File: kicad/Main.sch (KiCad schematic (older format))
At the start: 0 parts

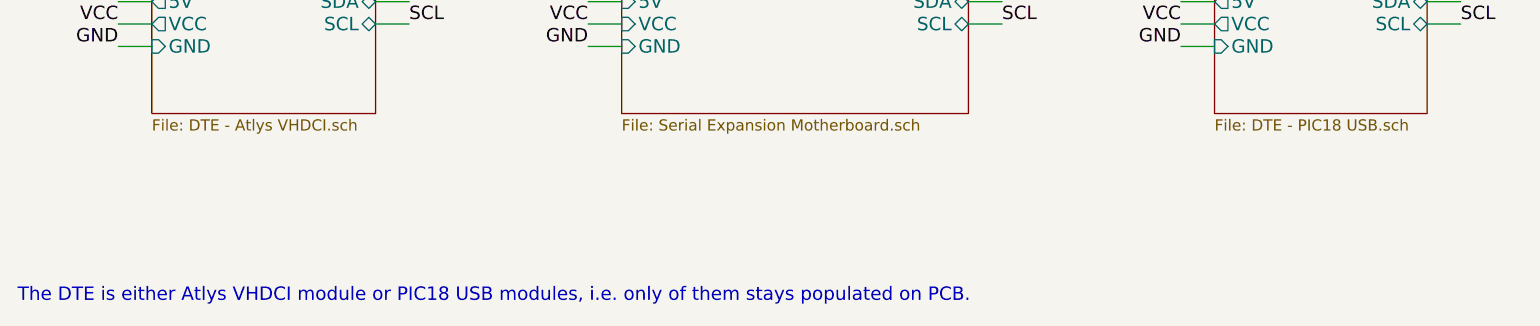
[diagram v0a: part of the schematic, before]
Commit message: ID controller complete, bypass caps added in data isolation
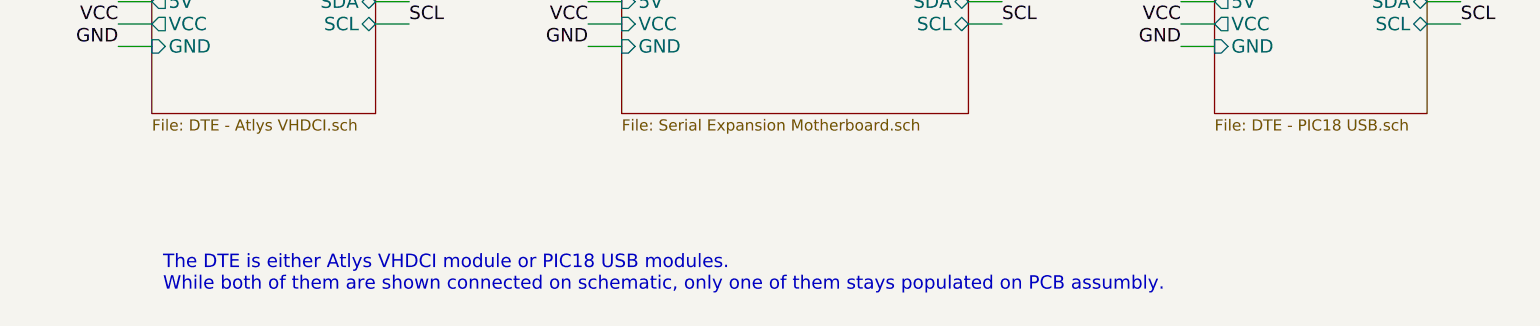
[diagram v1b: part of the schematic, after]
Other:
- note added: "The DTE is either Atlys VHDCI module or PIC18 USB modules.\nWhile both of them are shown connected on schematic, only one of them stays populated on PCB assumbly."
- note removed: "The DTE is either Atlys VHDCI module or PIC18 USB modules, i.e. only of them stays populated on PCB."
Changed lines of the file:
@@
 LIBS:roe-0505s
 LIBS:si8660
+LIBS:pic16f1704
 LIBS:Main-cache
 EELAYER 27 0
@@
 F42 "DSR5" O R 6900 4550 60
 $EndSheet
-Text Notes 2650 6100 0    60   ~ 0
-The DTE is either Atlys VHDCI module or PIC18 USB modules, i.e. only of them stays populated on PCB.
+Text Notes 3300 6050 0    60   ~ 0
+The DTE is either Atlys VHDCI module or PIC18 USB modules.\nWhile both of them are shown connected on schematic, only one of them stays populated on PCB assumbly.
 Wire Wire Line
 	5350 2650 5200 2650
